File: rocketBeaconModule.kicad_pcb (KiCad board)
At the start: 2 copper layers, 57.1 x 57.2 mm, 96 parts, among them J1 TYPE-C-31-M-12, J2 PWR, J3 GND, J4 PWR, J5 GND, U1 STM32F401CCU6, U2 CP2102N-Axx-xQFN20, U3 CC1200, U4 MCP6001-OT, U8 MCP41010, X1 40MHz, Y1 16MHz

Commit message: Revert "Stephen"
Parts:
- removed AE1: Antenna_Shield, Connector_Coaxial:SMA_BAT_Wireless_BWSMA-KWE-Z001
- removed C46: 0.1uF, Capacitor_SMD:C_0402_1005Metric
- removed C47: 10nF, Capacitor_SMD:C_0402_1005Metric
- removed JP1: SolderJumper_2_Open, Jumper:SolderJumper-2_P1.3mm_Open_RoundedPad1.0x1.5mm
- removed JP2: SolderJumper_2_Bridged, Jumper:SolderJumper-2_P1.3mm_Bridged_RoundedPad1.0x1.5mm
- removed L8: 22nH, Inductor_SMD:L_0402_1005Metric
- removed RFAMP1: RA07H4047M-101, RA07H4047M:RA07H4047M101_HORIZ
- removed RFSWITCH2: 4259-63, PE4259-63:SOT65P210X110-6N
- removed TH1: PT100, Resistor_SMD:R_0603_1608Metric
- removed U8: MCP41010, MCP41010:SOIC127P599X175-8N
- added C14: 10nF, Capacitor_SMD:C_0402_1005Metric, F.Cu at (58.7, 132.6)
- added C40: 1uF, Capacitor_SMD:C_0402_1005Metric, F.Cu at (59.9, 125.7)
- added C41: 1nF, Capacitor_SMD:C_0402_1005Metric, F.Cu at (60.7, 125.0)
- added C42: 10nF, Capacitor_SMD:C_0402_1005Metric, F.Cu at (62.2, 126.5)
- added D6: SS34, Diode_SMD:D_SMA, B.Cu at (62.4, 117.1)
- added J6: Conn_01x03_Pin, Connector_PinHeader_2.54mm:PinHeader_1x03_P2.54mm_Vertical, F.Cu at (47.9, 113.2)
- added P1: AntMount, Connector_Coaxial:SMA_Amphenol_132134-11_Vertical, F.Cu at (47.8, 126.7)
- added R15: 1k, Resistor_SMD:R_0402_1005Metric, F.Cu at (55.5, 117.0)
- added R17: 3.9k, Resistor_SMD:R_0402_1005Metric, B.Cu at (83.7, 114.6)
- added R18: 1k, Resistor_SMD:R_0402_1005Metric, B.Cu at (98.8, 116.0)
- C1, C2: footprint Capacitor_SMD:C_0402_1005Metric -> Capacitor_SMD:C_0603_1608Metric
- C21: value 1.5nF -> 1.8nF
- C31, C36: value 20pF -> 10pF
- C38, C39: value 0.1uF -> 220pF
- C43: value 100pF -> 220uF; footprint Capacitor_SMD:C_0402_1005Metric -> Capacitor_SMD:C_1206_3216Metric
- C44: value 100pF -> 10uF
- C45: value 100pF -> 100uF; footprint Capacitor_SMD:C_0402_1005Metric -> Capacitor_SMD:C_0805_2012Metric; moved to B.Cu
- L1, L2, L3, L4, L5, L6: footprint Inductor_SMD:L_0402_1005Metric -> Capacitor_SMD:C_0402_1005Metric
- L7: value 43nH -> 22nH; footprint Inductor_SMD:L_0402_1005Metric -> Capacitor_SMD:C_0402_1005Metric
- R1: moved to B.Cu
- R13, R8: footprint Resistor_SMD:R_0402_1005Metric -> Capacitor_SMD:C_0402_1005Metric
- R14: value 1000 -> 1k
- R16: value 1k -> 1.8k; moved to B.Cu
- R2: value 100 -> 0; footprint Resistor_SMD:R_0402_1005Metric -> Capacitor_SMD:C_0402_1005Metric
- R9: value 18 -> 18k; footprint Resistor_SMD:R_0402_1005Metric -> Capacitor_SMD:C_0402_1005Metric
- U4: value MCP6001-OT -> SKY65366-21; footprint Package_TO_SOT_SMD:SOT-23-5 -> SKY65366:SKY65366-21_SKY
- moved X1 134.3 mm to (63.5, 147.6), turned to -45 degrees
- moved C31 133.5 mm to (62.1, 149.4), turned to -45 degrees
- moved C28 132.5 mm to (64.7, 144.4), turned to 45 degrees
- moved C23 131.3 mm to (64.0, 143.8), turned to 45 degrees
- moved C29 131.3 mm to (63.8, 142.5), turned to 45 degrees
- moved C24 130.5 mm to (61.8, 139.6), turned to 180 degrees
- moved C36 130.3 mm to (65.5, 149.5), turned to -135 degrees
- moved C21 128.6 mm to (64.0, 140.3), turned to 180 degrees
- moved C25 128.4 mm to (66.0, 144.5), turned to 45 degrees
- moved C20 127.8 mm to (63.6, 138.6), turned to 0 degrees
- moved C18 124.7 mm to (67.9, 145.9), turned to 135 degrees
- moved C32 123.3 mm to (61.4, 137.3), turned to -45 degrees
- moved L2 123.0 mm to (65.2, 137.5), turned to -135 degrees
- moved U4 120.5 mm to (56.9, 128.6), turned to -45 degrees
- moved U3 120.1 mm to (68.8, 141.4), turned to 135 degrees
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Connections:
- C1 pad 1: +3.3V -> FEM_VPC
- C12 pad 1: +3.3V -> FEM_VPC
- C13 pad 1: +3.3V -> FEM_VPC
- C15 pad 1: +3.3V -> FEM_VPC
- C17 pad 1: +3.3V -> FEM_VPC
- C18 pad 1: +3.3V -> FEM_VPC
- C19 pad 1: +3.3V -> FEM_VPC
- C2 pad 1: +3.3V -> FEM_VPC
- C22 pad 1: +3.3V -> FEM_VPC
- C24 pad 1: +3.3V -> FEM_VPC
- C26 pad 2: +3.3V -> FEM_VPC
- C27 pad 1: +3.3V -> FEM_VPC
- C28 pad 2: +3.3V -> FEM_VPC
- C29 pad 2: +3.3V -> FEM_VPC
- C33 pad 1: /CC1200/RX -> Net-(C33-Pad1)
- C35 pad 1: Net-(U3-TRX_SW) -> Net-(C34-Pad1)
- C35 pad 2: Net-(C34-Pad1) -> GND
- C37 pad 1: Net-(C14-Pad1) -> Net-(C37-Pad1)
- C38 pad 1: TEMPSENSORADC -> FEM_VPC
- C39 pad 1: +3.3V -> GND
- C39 pad 2: GND -> +3V9
- C4 pad 1: +3.3V -> FEM_VPC
- C43 pad 1: /CC1200/TX -> GND
- C43 pad 2: Net-(RFSWITCH2-RFC) -> +3V9
- C44 pad 1: Net-(RFSWITCH2-RF2) -> GND
- C44 pad 2: Net-(RFAMP1-RF_INPUT_(PIN)) -> +3V9
- C45 pad 1: Net-(RFSWITCH2-RF1) -> GND
- C45 pad 2: Net-(AE1-A) -> /HV_SUPPLY
- C5 pad 1: +3.3V -> FEM_VPC
- C7 pad 1: +3.3V -> FEM_VPC
- C8 pad 1: +3.3V -> FEM_VPC
- D1 pad 2: +3.3V -> FEM_VPC
- EX1 pad 7: +3.3V -> FEM_VPC
- FB1 pad 2: +3.3V -> FEM_VPC
- J2 pad 1: +3.3V -> FEM_VPC
- L3 pad 2: /CC1200/RX -> Net-(C33-Pad1)
- L6 pad 1: Net-(U3-TRX_SW) -> Net-(C33-Pad1)
- L6 pad 2: /CC1200/RX -> Net-(U4-RX0)
- L7 pad 2: Net-(C14-Pad1) -> Net-(C37-Pad1)
- R1 pad 2: +3.3V -> FEM_VPC
- R10 pad 1: +3.3V -> FEM_VPC
- R11 pad 1: +3.3V -> FEM_VPC
- R12 pad 1: +3.3V -> FEM_VPC
- R13 pad 1: Net-(C14-Pad2) -> Net-(C37-Pad1)
- R13 pad 2: /CC1200/TX -> Net-(U4-TX)
- R14 pad 1: Net-(R14-Pad1) -> FEM_EN
- R14 pad 2: TEMPSENSORADC -> FEM_VPC
- R16 pad 1: VCTL -> GND
- R16 pad 2: +3.3V -> Net-(U5-FB)
- R2 pad 1: Net-(R14-Pad1) -> Net-(U4-RBIAS)
- R9 pad 2: +3.3V -> FEM_VPC
- SWD1 pad 1: +3.3V -> FEM_VPC
- U1 pad 1: +3.3V -> FEM_VPC
- U1 pad 10: TEMPSENSORADC -> unconnected-(U1-PA0-Pad10)
- U1 pad 19: VCTL -> unconnected-(U1-PB1-Pad19)
- U1 pad 21: AMP_ON -> unconnected-(U1-PB10-Pad21)
- U1 pad 24: +3.3V -> FEM_VPC
- U1 pad 36: +3.3V -> FEM_VPC
- U1 pad 39: SPICLK -> unconnected-(U1-PB3-Pad39)
- U1 pad 40: SPICS -> unconnected-(U1-PB4-Pad40)
- U1 pad 41: SPIDATA -> unconnected-(U1-PB5-Pad41)
- U1 pad 48: +3.3V -> FEM_VPC
- U2 pad 6: +3.3V -> FEM_VPC
- U3 pad 1: +3.3V -> FEM_VPC
- U3 pad 12: +3.3V -> FEM_VPC
- U3 pad 13: +3.3V -> FEM_VPC
- U3 pad 15: +3.3V -> FEM_VPC
- U3 pad 18: Net-(U3-TRX_SW) -> unconnected-(U3-TRX_SW-Pad18)
- U3 pad 22: +3.3V -> FEM_VPC
- U3 pad 25: +3.3V -> FEM_VPC
- U3 pad 27: +3.3V -> FEM_VPC
- U3 pad 28: +3.3V -> FEM_VPC
- U3 pad 5: +3.3V -> FEM_VPC
- U4 pad 1: Net-(RFAMP1-GATE_VOLTAGE_(VGG)) -> GND
- U4 pad 2: GND -> FEM_TR
- U4 pad 3: Net-(JP1-A) -> FEM_EN
- U4 pad 4: Net-(RFAMP1-GATE_VOLTAGE_(VGG)) -> FEM_BYP
- U4 pad 5: +3.3V -> FEM_VPC
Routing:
- net FEM_VPC: track 0.00 -> 301.6 mm, vias 0 -> 23
- net +3.3V: track 290.7 -> 0.00 mm, vias 18 -> 0
- net GND: track 134.3 -> 362.0 mm, vias 36 -> 128
- net +3V9: track 0.00 -> 70.7 mm, vias 0 -> 1
- net FEM_BYP: track 0.00 -> 60.6 mm, vias 0 -> 2
- net FEM_EN: track 0.00 -> 52.1 mm, vias 0 -> 2
- net FEM_TR: track 0.00 -> 49.9 mm, vias 0 -> 2
- net /LED1: track 13.4 -> 54.1 mm, vias 2 -> 4
- net SPICS: track 39.0 -> 0.00 mm, vias 2 -> 0
- net SPIDATA: track 38.6 -> 0.00 mm, vias 2 -> 0
- net Net-(D6-K): track 0.00 -> 37.0 mm
- net SPICLK: track 35.8 -> 0.00 mm, vias 2 -> 0
- net /LED2: track 15.1 -> 48.8 mm
- net /CP2102N_SIG2: track 53.6 -> 24.8 mm, vias 2 -> 4
- net Net-(AE1-A): track 28.1 -> 0.00 mm
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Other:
- board size 57.1 x 57.2 mm -> 57.2 x 57.2 mm
- board text added: "3V3"
- board text added: "60mm"
- board text added: "ArmstrongLabs"
- board text added: "BAT"
- board text added: "CIRCLE CENTER"
- board text added: "CIRCLE EDGE"
- board text added: "GND"
- board text added: "GND RST RX TX S2 S1 3V3 5V"
- board text added: "LED1"
- board text added: "LED2"
- board text added: "NRST"
- board text added: "PWR"
- board text added: "RX"
- board text added: "SWCLK"
- board text added: "SWDIO"
- board text added: "SubGhz Transciever"
- board text added: "TX"
- board text added: "USB"
- board text added: "V4"

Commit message: changed rf switch, updated rf amp footprint and updated schematic
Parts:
- removed C38, C39: 220pF, Capacitor_SMD:C_0402_1005Metric
- removed C40: 1uF, Capacitor_SMD:C_0402_1005Metric
- removed C41: 1nF, Capacitor_SMD:C_0402_1005Metric
- removed C42: 10nF, Capacitor_SMD:C_0402_1005Metric
- removed D6: SS34, Diode_SMD:D_SMA
- removed P1: AntMount, Connector_Coaxial:SMA_Amphenol_132134-11_Vertical
- removed R14, R15, R18: 1k, Resistor_SMD:R_0402_1005Metric
- removed R17: 3.9k, Resistor_SMD:R_0402_1005Metric
- removed R2: 0, Capacitor_SMD:C_0402_1005Metric
- added C46: 0.1uF, Capacitor_SMD:C_0402_1005Metric, F.Cu at (-19.3, 135.4)
- added C47: 10nF, Capacitor_SMD:C_0402_1005Metric, F.Cu at (-19.3, 137.4)
- added L8: 22nH, Inductor_SMD:L_0402_1005Metric, F.Cu at (-27.0, 121.2)
- added RFAMP1: RA07H4047M-101, RA07H4047M:RA07H4047M101, F.Cu at (-24.6, 94.4)
- added RFSWITCH2: 4259-63, PE4259-63:SOT65P210X110-6N, F.Cu at (-12.8, 136.8)
- C14: value 10nF -> DNM
- C21: value 1.8nF -> 1.5nF
- C31, C36: value 10pF -> 20pF
- C43: value 220uF -> 100pF; footprint Capacitor_SMD:C_1206_3216Metric -> Capacitor_SMD:C_0402_1005Metric
- C44: value 10uF -> 100pF
- C45: value 100uF -> 100pF; footprint Capacitor_SMD:C_0805_2012Metric -> Capacitor_SMD:C_0402_1005Metric; moved to F.Cu
- J6: value Conn_01x03_Pin -> SMA_CONNECTOR; footprint Connector_PinHeader_2.54mm:PinHeader_1x03_P2.54mm_Vertical -> Connector_Coaxial:SMA_Amphenol_901-143_Horizontal
- L1, L2, L3, L4, L5, L6: footprint Capacitor_SMD:C_0402_1005Metric -> Inductor_SMD:L_0402_1005Metric
- L7: value 22nH -> 43nH; footprint Capacitor_SMD:C_0402_1005Metric -> Inductor_SMD:L_0402_1005Metric
- R1: moved to F.Cu
- R13, R8: footprint Capacitor_SMD:C_0402_1005Metric -> Resistor_SMD:R_0402_1005Metric
- R16: value 1.8k -> 1k; moved to F.Cu
- R9: value 18k -> 18; footprint Capacitor_SMD:C_0402_1005Metric -> Resistor_SMD:R_0402_1005Metric
- U4: value SKY65366-21 -> MCP6001-OT; footprint SKY65366:SKY65366-21_SKY -> Package_TO_SOT_SMD:SOT-23-5
- moved R16 100.7 mm to (-16.4, 133.2), turned to 0 degrees
- moved C34 96.1 mm to (-29.9, 123.2), turned to 0 degrees
- moved C35 93.7 mm to (-29.9, 125.2), turned to 0 degrees
- moved C14 89.3 mm to (-29.9, 121.2), turned to 0 degrees
- moved C45 86.7 mm to (-19.3, 133.5), turned to 0 degrees
- moved J6 86.4 mm to (-36.2, 132.8), turned to 0 degrees
- moved C43 84.0 mm to (-19.3, 129.5), turned to 0 degrees
- moved C44 81.1 mm to (-19.3, 131.5), turned to 0 degrees
- moved U4 80.1 mm to (-23.0, 122.6), turned to 0 degrees
- moved R13 79.9 mm to (-18.4, 124.6), turned to 0 degrees
- moved R1 0.69 mm to (83.5, 131.6), turned to -179.2 degrees
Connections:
- C1 pad 1: FEM_VPC -> +3.3V
- C12 pad 1: FEM_VPC -> +3.3V
- C13 pad 1: FEM_VPC -> +3.3V
- C14 pad 1: FEM_VPC -> Net-(C14-Pad1)
- C14 pad 2: GND -> Net-(C14-Pad2)
- C15 pad 1: FEM_VPC -> +3.3V
- C17 pad 1: FEM_VPC -> +3.3V
- C18 pad 1: FEM_VPC -> +3.3V
- C19 pad 1: FEM_VPC -> +3.3V
- C2 pad 1: FEM_VPC -> +3.3V
- C22 pad 1: FEM_VPC -> +3.3V
- C24 pad 1: FEM_VPC -> +3.3V
- C26 pad 2: FEM_VPC -> +3.3V
- C27 pad 1: FEM_VPC -> +3.3V
- C28 pad 2: FEM_VPC -> +3.3V
- C29 pad 2: FEM_VPC -> +3.3V
- C33 pad 1: Net-(C33-Pad1) -> /CC1200/RX
- C35 pad 1: Net-(C34-Pad1) -> Net-(U3-TRX_SW)
- C35 pad 2: GND -> Net-(C34-Pad1)
- C37 pad 1: Net-(C37-Pad1) -> Net-(C14-Pad1)
- C4 pad 1: FEM_VPC -> +3.3V
- C43 pad 1: GND -> /CC1200/TX
- C43 pad 2: +3V9 -> Net-(RFSWITCH2-RFC)
- C44 pad 1: GND -> Net-(RFSWITCH2-RF2)
- C44 pad 2: +3V9 -> Net-(RFAMP1-RF_INPUT_(PIN))
- C45 pad 1: GND -> Net-(RFSWITCH2-RF1)
- C45 pad 2: /HV_SUPPLY -> Net-(AE1-A)
- C5 pad 1: FEM_VPC -> +3.3V
- C7 pad 1: FEM_VPC -> +3.3V
- C8 pad 1: FEM_VPC -> +3.3V
- D1 pad 2: FEM_VPC -> +3.3V
- EX1 pad 7: FEM_VPC -> +3.3V
- FB1 pad 2: FEM_VPC -> +3.3V
- J2 pad 1: FEM_VPC -> +3.3V
- J6 pad 1: +BATT -> Net-(RFAMP1-RF_OUTPUT_(POUT))
- J6 pad 2: /HV_SUPPLY -> (no net)
- L3 pad 2: Net-(C33-Pad1) -> /CC1200/RX
- L6 pad 1: Net-(C33-Pad1) -> Net-(U3-TRX_SW)
- L6 pad 2: Net-(U4-RX0) -> /CC1200/RX
- L7 pad 2: Net-(C37-Pad1) -> Net-(C14-Pad1)
- R1 pad 2: FEM_VPC -> +3.3V
- R10 pad 1: FEM_VPC -> +3.3V
- R11 pad 1: FEM_VPC -> +3.3V
- R12 pad 1: FEM_VPC -> +3.3V
- R13 pad 1: Net-(C37-Pad1) -> Net-(C14-Pad2)
- R13 pad 2: Net-(U4-TX) -> /CC1200/TX
- R16 pad 1: GND -> VCTL
- R16 pad 2: Net-(U5-FB) -> +3.3V
- R9 pad 2: FEM_VPC -> +3.3V
- SWD1 pad 1: FEM_VPC -> +3.3V
- U1 pad 1: FEM_VPC -> +3.3V
- U1 pad 19: unconnected-(U1-PB1-Pad19) -> VCTL
- U1 pad 24: FEM_VPC -> +3.3V
- U1 pad 36: FEM_VPC -> +3.3V
- U1 pad 48: FEM_VPC -> +3.3V
- U2 pad 6: FEM_VPC -> +3.3V
- U3 pad 1: FEM_VPC -> +3.3V
- U3 pad 12: FEM_VPC -> +3.3V
- U3 pad 13: FEM_VPC -> +3.3V
- U3 pad 15: FEM_VPC -> +3.3V
- U3 pad 18: unconnected-(U3-TRX_SW-Pad18) -> Net-(U3-TRX_SW)
- U3 pad 22: FEM_VPC -> +3.3V
- U3 pad 25: FEM_VPC -> +3.3V
- U3 pad 27: FEM_VPC -> +3.3V
- U3 pad 28: FEM_VPC -> +3.3V
- U3 pad 5: FEM_VPC -> +3.3V
- U4 pad 1: GND -> Net-(RFAMP1-GATE_VOLTAGE_(VGG))
- U4 pad 2: FEM_TR -> GND
- U4 pad 3: FEM_EN -> Net-(JP1-A)
- U4 pad 4: FEM_BYP -> Net-(RFAMP1-GATE_VOLTAGE_(VGG))
- U4 pad 5: FEM_VPC -> +3.3V
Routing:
- net +3.3V: track 0.00 -> 304.8 mm, vias 0 -> 24
- net FEM_VPC: track 301.6 -> 0.00 mm, vias 23 -> 0
- net (no net): track 0.00 -> 126.1 mm
- net +3V9: track 70.7 -> 0.00 mm, vias 1 -> 0
- net GND: track 362.0 -> 314.5 mm, vias 128 -> 112
- net Net-(D6-K): track 37.0 -> 0.00 mm
- net Net-(U5-FB): track 27.4 -> 0.00 mm
- net /HV_SUPPLY: track 24.1 -> 0.00 mm
- net Net-(P1-Pin_1): track 6.26 -> 0.00 mm
- net Net-(U4-RX0): track 5.70 -> 0.00 mm
- net /CC1200/RX: track 0.00 -> 5.70 mm
- net Net-(U4-RX1): track 3.37 -> 0.00 mm
- net VCTL: track 0.00 -> 2.30 mm
- net Net-(C33-Pad1): track 2.19 -> 0.00 mm
- net Net-(RFSWITCH2-RFC): track 0.00 -> 2.12 mm
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
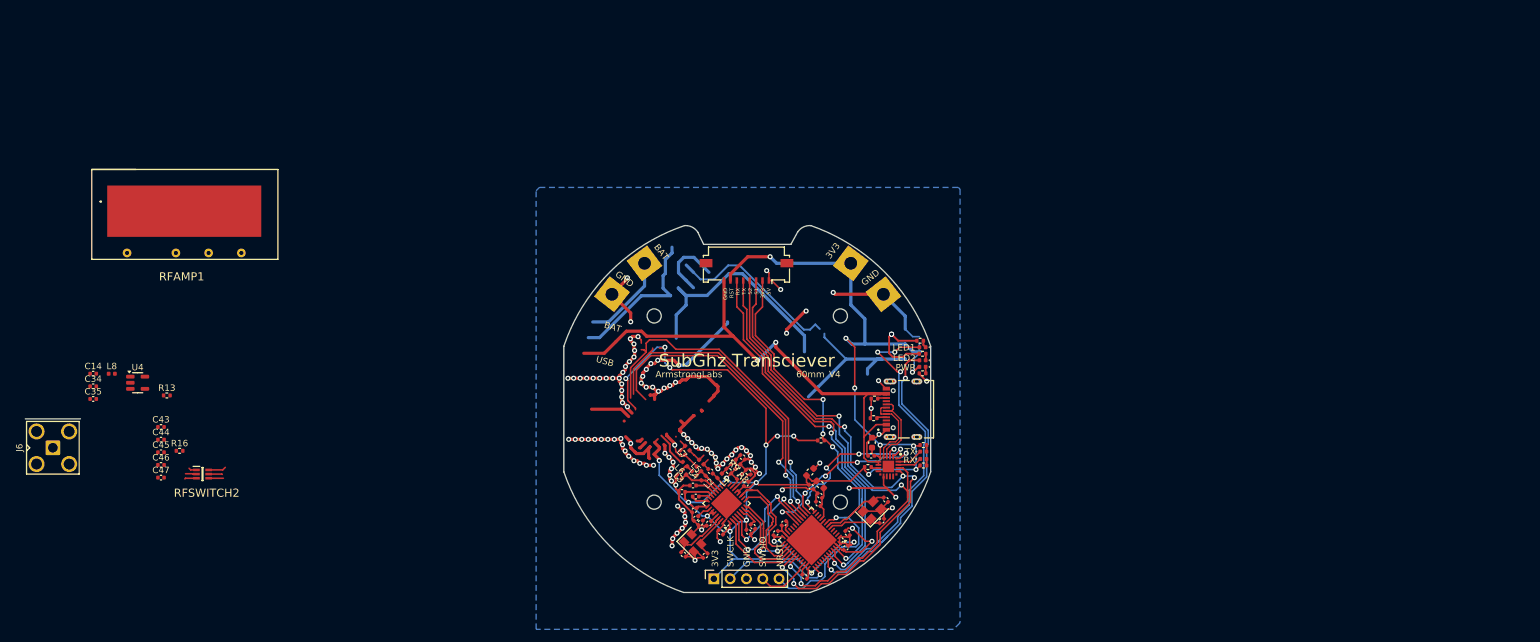
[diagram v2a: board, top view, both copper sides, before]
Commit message: reference/backup for mostly routed pcb
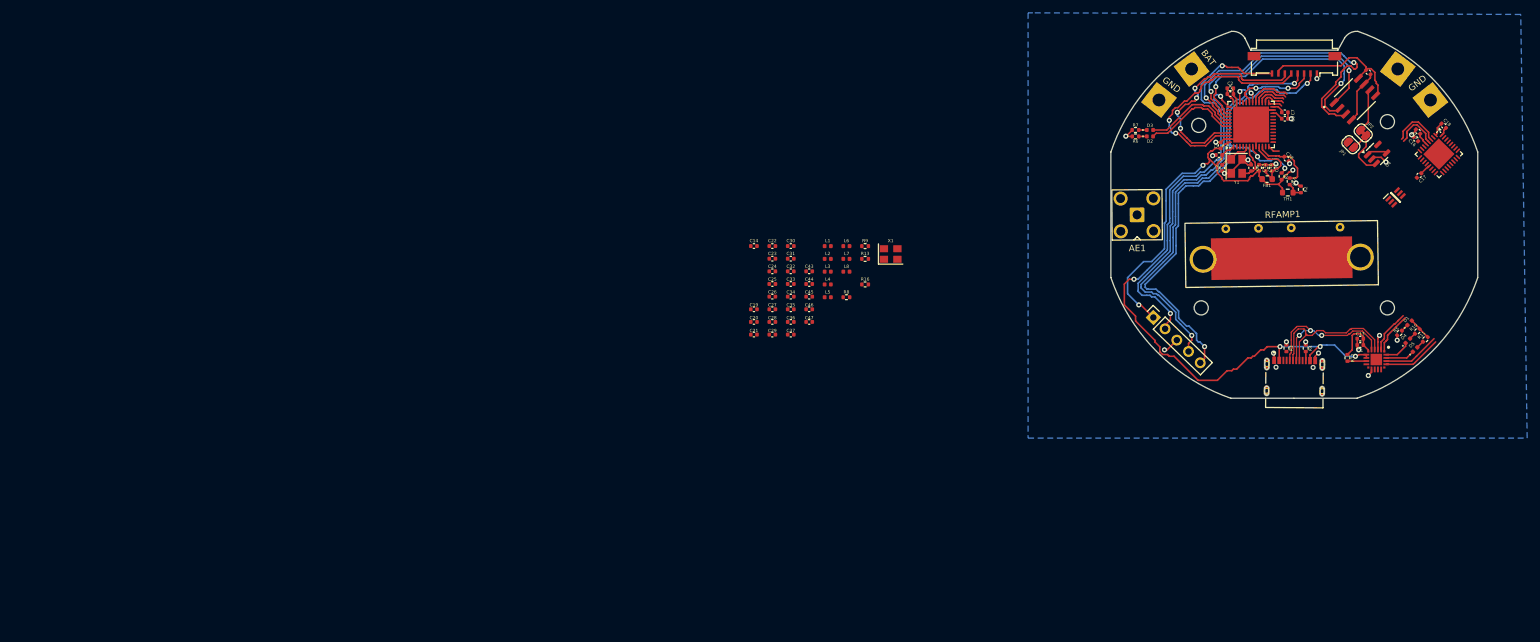
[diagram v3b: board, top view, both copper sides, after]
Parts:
- removed J6: SMA_CONNECTOR, Connector_Coaxial:SMA_Amphenol_901-143_Horizontal
- added AE1: Antenna_Shield, Connector_Coaxial:SMA_BAT_Wireless_BWSMA-KWE-Z001, F.Cu at (132.7, 96.5)
- added C38: 0.1uF, Capacitor_SMD:C_0402_1005Metric, F.Cu at (156.0, 87.8)
- added C39: 0.1uF, Capacitor_SMD:C_0402_1005Metric, F.Cu at (168.8, 74.2)
- added JP1: SolderJumper_2_Open, Jumper:SolderJumper-2_P1.3mm_Open_RoundedPad1.0x1.5mm, F.Cu at (166.0, 85.5)
- added JP2: SolderJumper_2_Bridged, Jumper:SolderJumper-2_P1.3mm_Bridged_RoundedPad1.0x1.5mm, F.Cu at (168.0, 83.7)
- added R14: 1000, Resistor_SMD:R_0402_1005Metric, F.Cu at (156.5, 91.2)
- added R2: 100, Resistor_SMD:R_0402_1005Metric, F.Cu at (158.2, 92.5)
- added TH1: PT100, Resistor_SMD:R_0603_1608Metric, F.Cu at (156.2, 93.0)
- added U8: MCP41010, MCP41010:SOIC127P599X175-8N, F.Cu at (166.7, 78.4)
- C1, C2: footprint Capacitor_SMD:C_0603_1608Metric -> Capacitor_SMD:C_0402_1005Metric
- RFAMP1: footprint RA07H4047M:RA07H4047M101 -> RA07H4047M:RA07H4047M101_HORIZ
- moved U4 196.3 mm to (170.1, 87.0), turned to 45 degrees
- moved RFSWITCH2 190.8 mm to (173.0, 93.8), turned to 45 degrees
- moved RFAMP1 182.6 mm to (155.8, 122.8), turned to -179.199 degrees
- moved C18 129.2 mm to (180.5, 82.6), turned to -45 degrees
- moved U3 123.6 mm to (179.8, 87.0), turned to -44.4 degrees
- moved C15 121.5 mm to (176.5, 83.5), turned to 135 degrees
- moved C16 119.6 mm to (176.2, 84.7), turned to 135 degrees
- moved L8 115.5 mm to (87.5, 105.3)
- moved C17 115.3 mm to (176.7, 90.3), turned to -135 degrees
- moved R13 110.8 mm to (90.4, 103.3)
- moved R16 109.9 mm to (90.4, 107.3)
- moved C34 109.6 mm to (78.8, 109.2)
- moved C35 109.6 mm to (78.8, 111.2)
- moved C14 104.8 mm to (73.0, 101.3)
- moved C43 103.8 mm to (81.7, 105.3)
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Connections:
- U1 pad 10: unconnected-(U1-PA0-Pad10) -> TEMPSENSORADC
- U1 pad 39: unconnected-(U1-PB3-Pad39) -> SPICLK
- U1 pad 40: unconnected-(U1-PB4-Pad40) -> SPICS
- U1 pad 41: unconnected-(U1-PB5-Pad41) -> SPIDATA
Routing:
- net GND: track 314.5 -> 66.3 mm, vias 112 -> 21
- net +3.3V: track 304.8 -> 109.1 mm, vias 24 -> 3
- net (no net): track 126.1 -> 0.00 mm
- net /TX: track 85.9 -> 21.4 mm, vias 5 -> 2
- net /RX: track 84.8 -> 22.0 mm, vias 4 -> 2
- net FEM_BYP: track 58.7 -> 0.00 mm, vias 2 -> 0
- net FEM_EN: track 50.2 -> 0.00 mm, vias 2 -> 0
- net FEM_TR: track 49.9 -> 0.00 mm, vias 2 -> 0
- net SPIDATA: track 0.00 -> 48.7 mm, vias 0 -> 2
- net /SWDIO: track 8.60 -> 56.8 mm, vias 0 -> 2
- net /LED1: track 54.1 -> 15.1 mm, vias 4 -> 0
- net SPICLK: track 0.00 -> 38.4 mm, vias 0 -> 2
- net SPICS: track 0.00 -> 37.5 mm, vias 0 -> 2
- net /LED2: track 48.8 -> 14.9 mm, vias 2 -> 0
- net /SWCLK: track 17.7 -> 51.0 mm, vias 1 -> 2
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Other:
- board size 57.2 x 57.2 mm -> 57.1 x 57.2 mm
- board text removed: "3V3"
- board text removed: "60mm"
- board text removed: "ArmstrongLabs"
- board text removed: "CIRCLE CENTER"
- board text removed: "CIRCLE EDGE"
- board text removed: "GND RST RX TX S2 S1 3V3 5V"
- board text removed: "LED1"
- board text removed: "LED2"
- board text removed: "NRST"
- board text removed: "PWR"
- board text removed: "RX"
- board text removed: "SWCLK"
- board text removed: "SWDIO"
- board text removed: "SubGhz Transciever"
- board text removed: "TX"
- board text removed: "USB"
- board text removed: "V4"
